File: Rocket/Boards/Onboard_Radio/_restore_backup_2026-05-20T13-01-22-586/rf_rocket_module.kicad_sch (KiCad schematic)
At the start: 13 parts

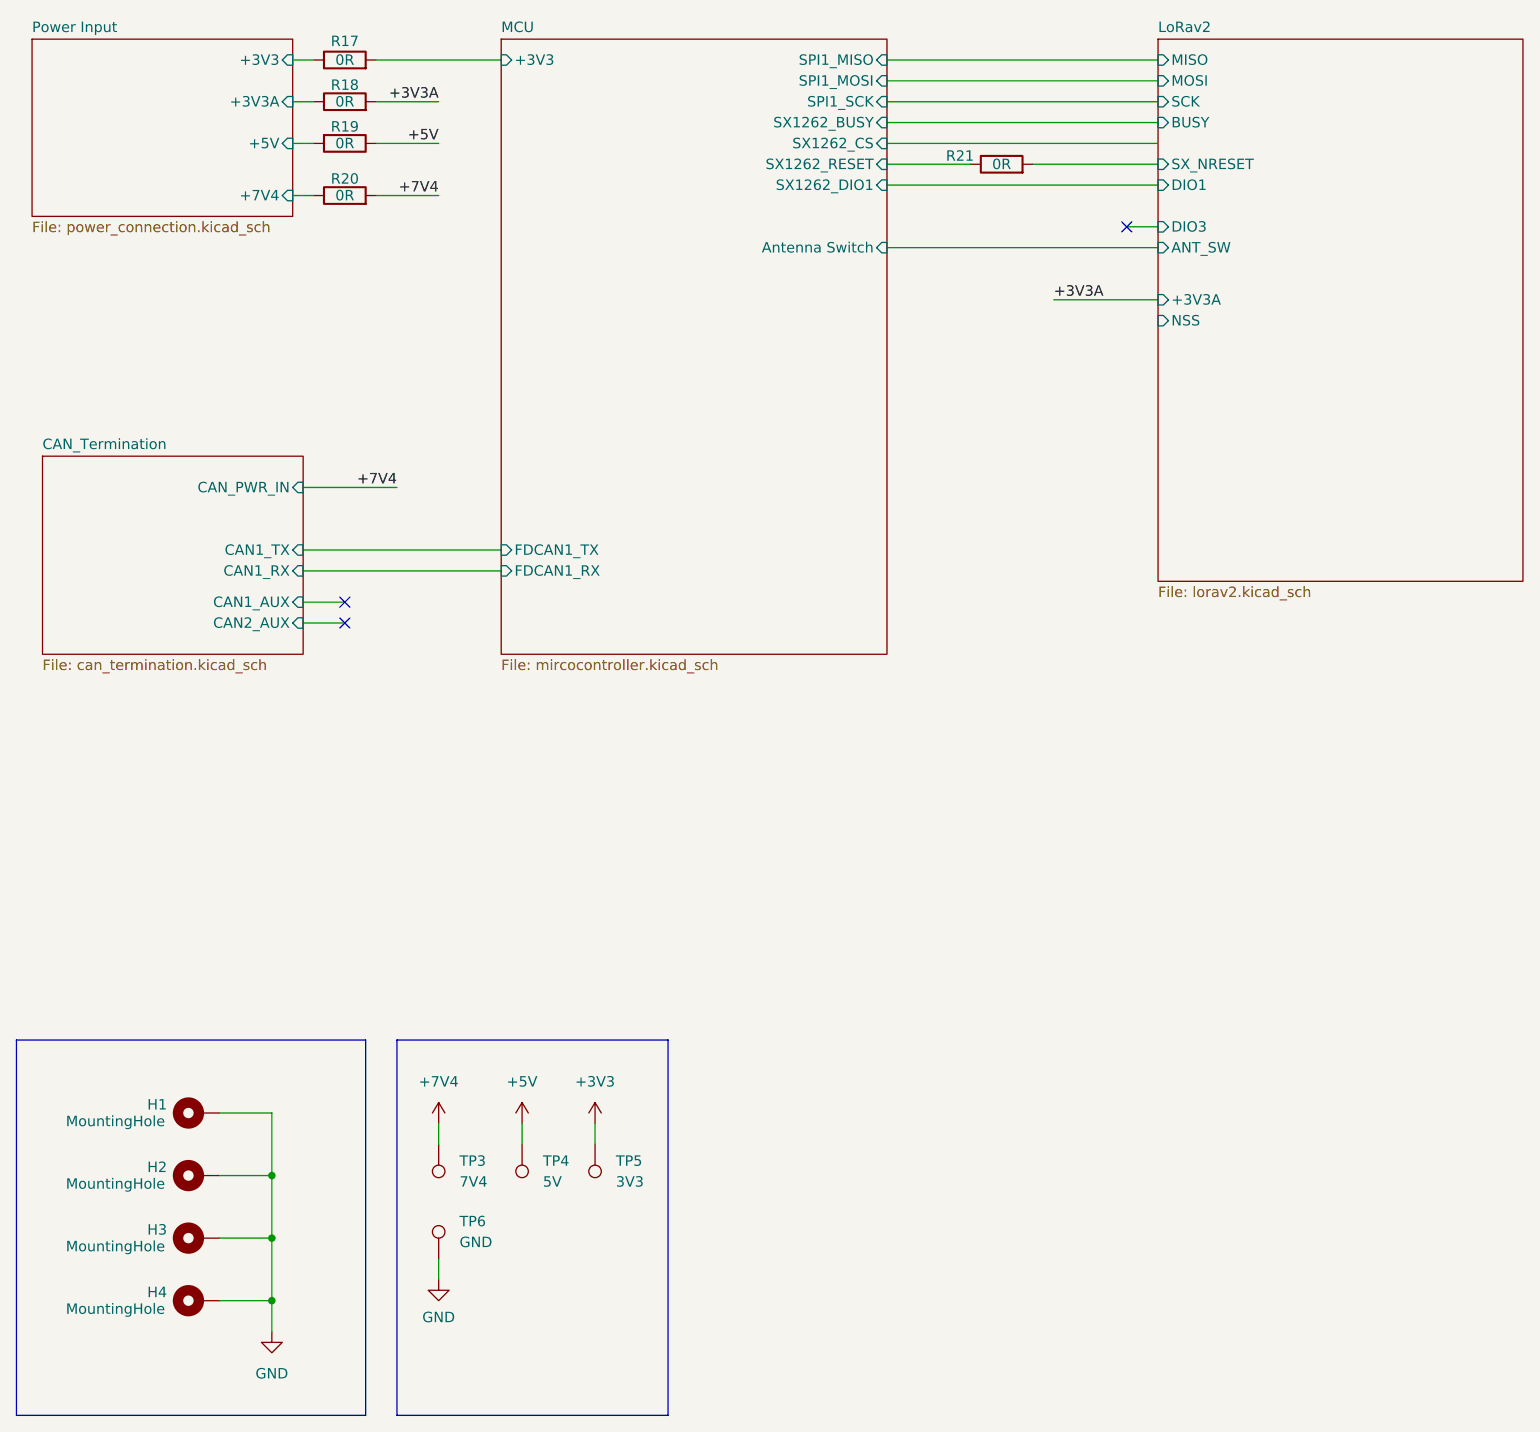
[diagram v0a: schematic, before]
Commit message: schematic bom needs updating and traces need finishing
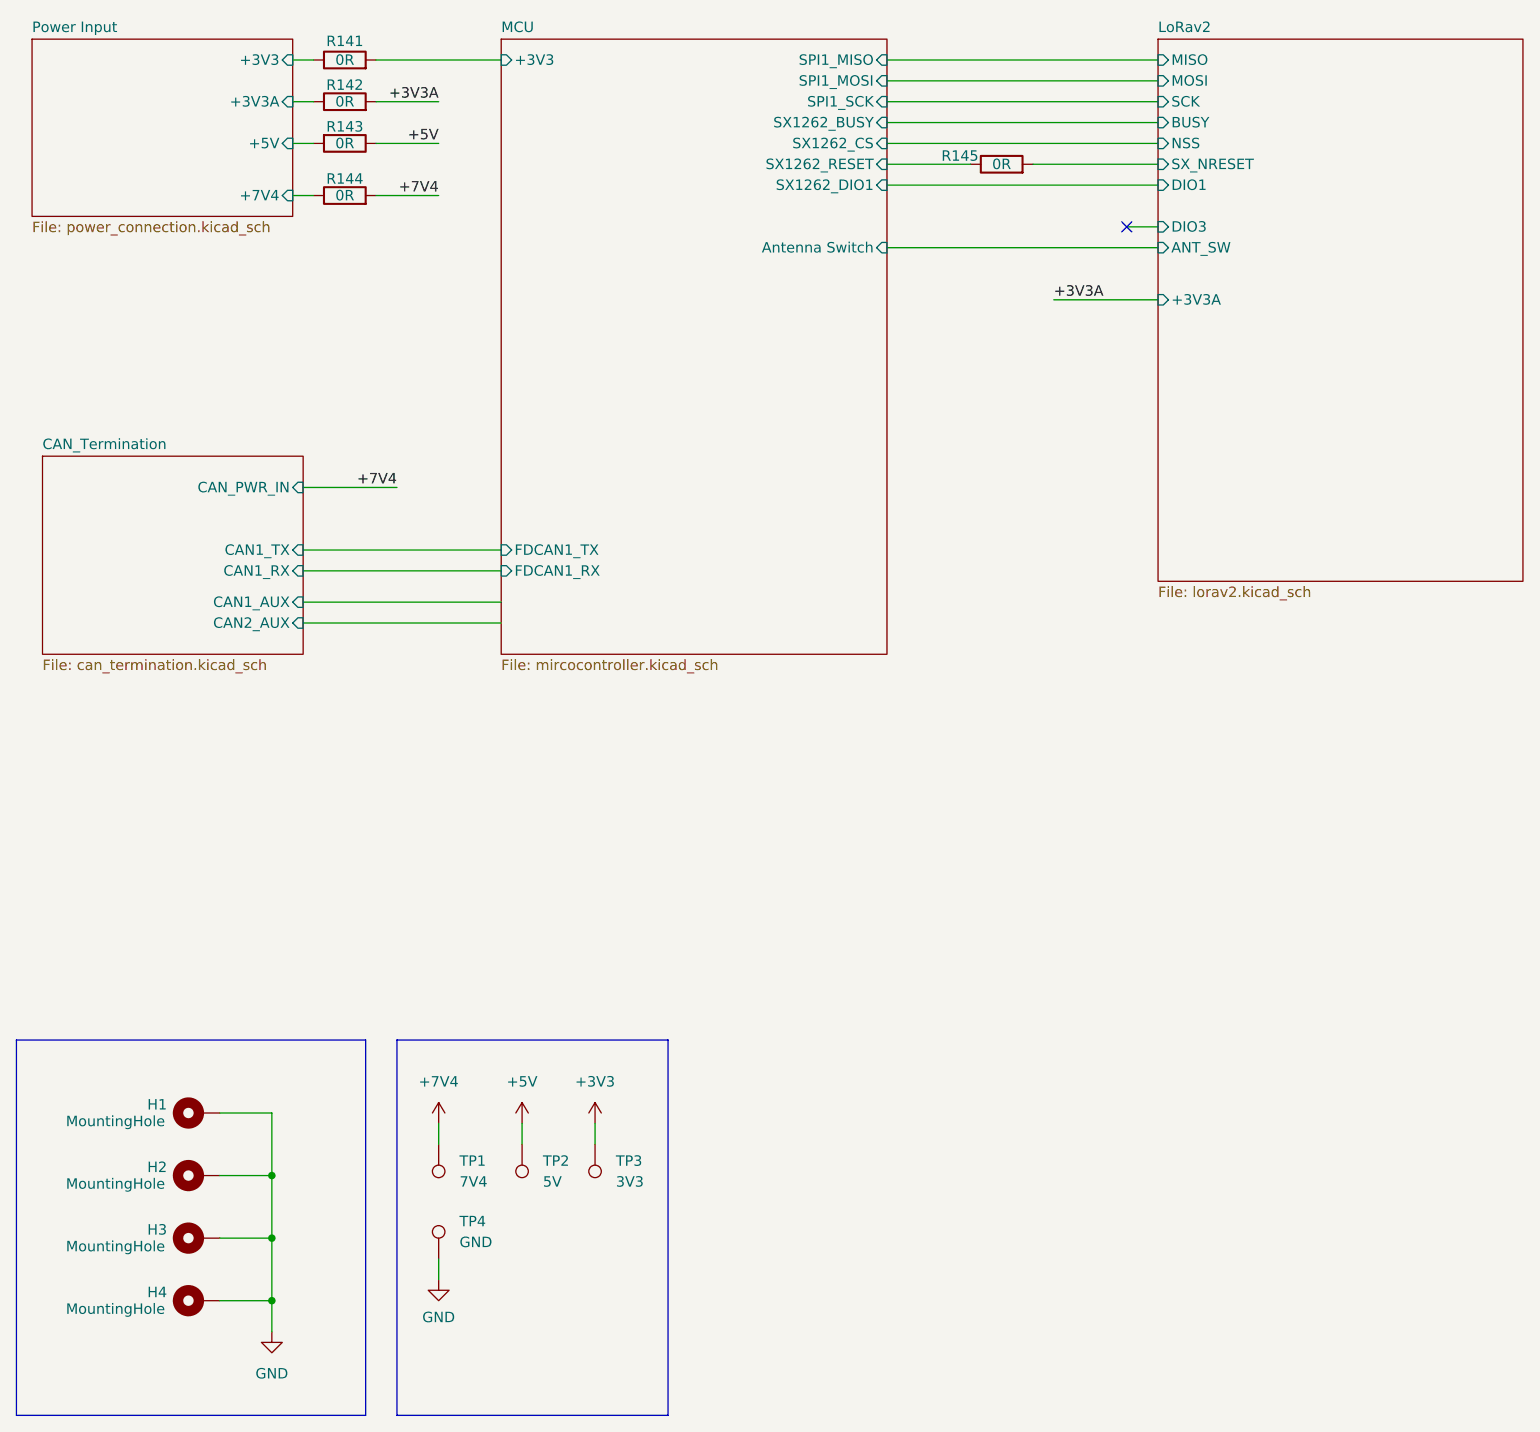
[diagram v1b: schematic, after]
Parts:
- renumbered R17 to R141, R18 to R142, R19 to R143, R20 to R144, R21 to R145, TP3 to TP1, TP4 to TP2, TP5 to TP3, TP6 to TP4
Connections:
- no-connect marks 3 -> 1
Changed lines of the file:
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@@
-	)
-	(no_connect
-		(at 58.42 88.9)
 	)
 	(no_connect
 		(at 153.67 43.18)
 	)
-	(no_connect
-		(at 58.42 91.44)
+	(wire
+		(pts
+			(xy 53.34 88.9) (xy 77.47 88.9)
+		)
+		(stroke
+			(width 0)
+			(type default)
+		)
 	)
 	(wire
@@
 	(wire
 		(pts
-			(xy 53.34 88.9) (xy 58.42 88.9)
-		)
-		(stroke
-			(width 0)
-			(type default)
-		)
-	)
-	(wire
-		(pts
 			(xy 69.85 152.4) (xy 69.85 154.94)
 		)
@@
 	(wire
 		(pts
-			(xy 53.34 91.44) (xy 58.42 91.44)
+			(xy 53.34 91.44) (xy 77.47 91.44)
 		)
 		(stroke
@@
 		(in_pos_files yes)
 		(dnp no)
-		(property "Reference" "R21"
+		(property "Reference" "R145"
 			(at 133.35 34.544 90)
 			(show_name no)
@@
 			(project "rf_rocket_module"
 				(path "/4940ffbe-f45f-4917-a247-12e2b32b6c35"
-					(reference "R21")
+					(reference "R145")
 					(unit 1)
 				)
@@
 		(in_pos_files yes)
 		(dnp no)
-		(property "Reference" "R19"
+		(property "Reference" "R143"
 			(at 58.42 30.988 90)
 			(show_name no)
@@
 			(project "rf_rocket_module"
 				(path "/4940ffbe-f45f-4917-a247-12e2b32b6c35"
-					(reference "R19")
+					(reference "R143")
 					(unit 1)
 				)
@@
 		(dnp no)
 		(fields_autoplaced yes)
-		(property "Reference" "TP4"
+		(property "Reference" "TP2"
 			(at 82.55 156.9719 0)
 			(show_name no)
@@
 			(project "rf_rocket_module"
 				(path "/4940ffbe-f45f-4917-a247-12e2b32b6c35"
-					(reference "TP4")
+					(reference "TP2")
 					(unit 1)
 				)
@@
 		(exclude_from_sim no)
 		(in_bom no)
-		(on_board no)
+		(on_board yes)
 		(in_pos_files yes)
 		(dnp no)
@@
 		(dnp no)
 		(fields_autoplaced yes)
-		(property "Reference" "TP5"
+		(property "Reference" "TP3"
 			(at 91.44 156.9719 0)
 			(show_name no)
@@
 			(project "rf_rocket_module"
 				(path "/4940ffbe-f45f-4917-a247-12e2b32b6c35"
-					(reference "TP5")
+					(reference "TP3")
 					(unit 1)
 				)
@@
 		(in_pos_files yes)
 		(dnp no)
-		(property "Reference" "R18"
+		(property "Reference" "R142"
 			(at 58.42 25.908 90)
 			(show_name no)
@@
 			(project "rf_rocket_module"
 				(path "/4940ffbe-f45f-4917-a247-12e2b32b6c35"
-					(reference "R18")
+					(reference "R142")
 					(unit 1)
 				)
@@
 		(exclude_from_sim no)
 		(in_bom no)
-		(on_board no)
+		(on_board yes)
 		(in_pos_files yes)
 		(dnp no)
@@
 		(in_pos_files yes)
 		(dnp no)
-		(property "Reference" "R17"
+		(property "Reference" "R141"
 			(at 58.42 20.574 90)
 			(show_name no)
@@
 			(project "rf_rocket_module"
 				(path "/4940ffbe-f45f-4917-a247-12e2b32b6c35"
-					(reference "R17")
+					(reference "R141")
 					(unit 1)
 				)
@@
 		(exclude_from_sim no)
 		(in_bom no)
-		(on_board no)
+		(on_board yes)
 		(in_pos_files yes)
 		(dnp no)
@@
 		(dnp no)
 		(fields_autoplaced yes)
-		(property "Reference" "TP3"
+		(property "Reference" "TP1"
 			(at 72.39 156.9719 0)
 			(show_name no)
@@
 			(project "rf_rocket_module"
 				(path "/4940ffbe-f45f-4917-a247-12e2b32b6c35"
-					(reference "TP3")
+					(reference "TP1")
 					(unit 1)
 				)
@@
 		(dnp no)
 		(fields_autoplaced yes)
-		(property "Reference" "TP6"
+		(property "Reference" "TP4"
 			(at 72.39 164.3379 0)
 			(show_name no)
@@
 			(project "rf_rocket_module"
 				(path "/4940ffbe-f45f-4917-a247-12e2b32b6c35"
-					(reference "TP6")
+					(reference "TP4")
 					(unit 1)
 				)
@@
 		(in_pos_files yes)
 		(dnp no)
-		(property "Reference" "R20"
+		(property "Reference" "R144"
 			(at 58.42 37.338 90)
 			(show_name no)
@@
 			(project "rf_rocket_module"
 				(path "/4940ffbe-f45f-4917-a247-12e2b32b6c35"
-					(reference "R20")
+					(reference "R144")
 					(unit 1)
 				)
@@
 		(exclude_from_sim no)
 		(in_bom no)
-		(on_board no)
+		(on_board yes)
 		(in_pos_files yes)
 		(dnp no)
@@
 			)
 		)
+		(pin "SX_NRESET" input
+			(at 157.48 35.56 180)
+			(effects
+				(font
+					(size 1.27 1.27)
+				)
+				(justify left)
+			)
+		)
 		(pin "DIO3" input
 			(at 157.48 43.18 180)
@@
 			)
 		)
+		(pin "NSS" input
+			(at 157.48 33.02 180)
+			(effects
+				(font
+					(size 1.27 1.27)
+				)
+				(justify left)
+			)
+		)
 		(pin "BUSY" input
 			(at 157.48 30.48 180)
@@
 			(effects
 				(font
-					(size 1.27 1.27)
-				)
-				(justify left)
-			)
-		)
-		(pin "NSS" input
-			(at 157.48 54.61 180)
-			(effects
-				(font
-					(size 1.27 1.27)
-				)
-				(justify left)
-			)
-		)
-		(pin "SX_NRESET" input
-			(at 157.48 35.56 180)
-			(effects
-				(font
